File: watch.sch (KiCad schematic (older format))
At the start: 22 parts, among them P1 CONN_6, SW1 SW_PUSH, SW2 SW_PUSH, SW3 SW_PUSH, SW4 SW_PUSH, U1 nrf51822, U3 S25FL1-K, X1 16MHz, X2 32.768kHz

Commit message: Added .gitignore, finished midmount layout
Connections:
- net +3.3V: now also SW1.1, SW3.1; no longer SW1.2, SW3.2
- net CS_DISP: now also U1.10 (GPIO6/AIN7/AREF1); no longer U1.9 (GPIO5/AIN6)
- net CS_MEM: now also U1.48 (GPIO29); no longer U1.47 (GPIO28)
- net DC_DISP: now also U1.9 (GPIO5/AIN6); no longer U1.8 (GPIO4/AIN5)
- net DISP_EN: now also U1.11 (GPIO7); no longer U1.17 (GPIO11)
- net HOLD_MEM: now also U1.47 (GPIO28); no longer U1.48 (GPIO29)
- net MCU_CTS: now also U1.21 (GPIO15); no longer U1.25 (GPIO17)
- net MCU_RTS: now also U1.19 (GPIO13); no longer U1.18 (GPIO12)
- net MCU_RX: now also U1.22 (GPIO16); no longer U1.26 (GPIO18)
- net MCU_TX: now also U1.20 (GPIO14); no longer U1.22 (GPIO16)
- net MOSI: now also U1.6 (GPIO2/AIN3); no longer U1.3 (GPIO30)
- net RST_DISP: now also U1.8 (GPIO4/AIN5); no longer U1.7 (GPIO3/AIN4)
- net SCK: now also U1.7 (GPIO3/AIN4); no longer U1.4 (GPIO0/AREF0)
- net SW1: now also SW1.2, U1.17 (GPIO11); no longer SW1.1, U1.14 (GPIO8)
- net SW2: now also U1.4 (GPIO0/AREF0); no longer U1.6 (GPIO2/AIN3)
- net SW3: now also SW3.2, U1.18 (GPIO12); no longer SW3.1, U1.15 (GPIO9)
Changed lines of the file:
@@
 Text Label 5900 1950 0    60   ~ 0
 MISO
-Text Label 5900 1850 0    60   ~ 0
+Text Label 5900 1750 0    60   ~ 0
 CS_MEM
 Text Label 8150 1850 2    60   ~ 0
@@
 Text Label 9250 1750 0    60   ~ 0
 MISO
-Text Label 5900 1750 0    60   ~ 0
+Text Label 5900 1850 0    60   ~ 0
 HOLD_MEM
 Text Label 9250 1950 0    60   ~ 0
@@
 F 3 "" H 8600 5150 60  0000 C CNN
 	1    8600 5150
-	1    0    0    -1
+	-1   0    0    -1
 $EndComp
 $Comp
@@
 F 3 "" H 8600 5800 60  0000 C CNN
 	1    8600 5800
-	1    0    0    -1
+	-1   0    0    -1
 $EndComp
 $Comp
@@
 Text Label 8300 6100 2    60   ~ 0
 SW4
-Text Label 5900 3650 0    60   ~ 0
+Text Label 5900 3350 0    60   ~ 0
 SW1
-Text Label 5900 4150 0    60   ~ 0
+Text Label 5900 4550 0    60   ~ 0
 SW2
-Text Label 5900 3550 0    60   ~ 0
+Text Label 5900 3250 0    60   ~ 0
 SW3
 Text Label 5900 2150 0    60   ~ 0
@@
 Wire Wire Line
 	6500 5350 6500 4250
-Wire Wire Line
-	6500 4250 5900 4250
 Connection ~ 7000 5350
 $Comp
@@
 Wire Wire Line
 	6000 6900 6000 7200
-Text GLabel 6700 2650 2    60   Input ~ 0
+Text GLabel 6150 2950 2    60   Input ~ 0
 MCU_CTS
-Text GLabel 6700 3250 2    60   Input ~ 0
+Text GLabel 6150 3150 2    60   Input ~ 0
 MCU_RTS
-Text GLabel 6700 2800 2    60   Input ~ 0
+Text GLabel 6150 3050 2    60   Input ~ 0
 MCU_TX
-Text GLabel 6700 2500 2    60   Input ~ 0
+Text GLabel 6150 2850 2    60   Input ~ 0
 MCU_RX
 $Sheet
@@
 	1    0    0    -1
 $EndComp
+Text GLabel 6150 3850 2    60   Input ~ 0
+DC_DISP
 Text GLabel 6150 3950 2    60   Input ~ 0
-DC_DISP
+RST_DISP
+Text GLabel 6150 4450 2    60   Input ~ 0
+CS_DISP
+Wire Wire Line
+	6150 3950 5900 3950
+Wire Wire Line
+	5900 3850 6150 3850
 Text GLabel 6150 4050 2    60   Input ~ 0
-RST_DISP
-Text GLabel 6150 3850 2    60   Input ~ 0
-CS_DISP
+SCK
+Text GLabel 6150 4150 2    60   Input ~ 0
+MOSI
 Wire Wire Line
 	6150 4050 5900 4050
 Wire Wire Line
-	5900 3950 6150 3950
-Text GLabel 6150 4550 2    60   Input ~ 0
-SCK
-Text GLabel 6150 4350 2    60   Input ~ 0
-MOSI
-Wire Wire Line
-	6150 4550 5900 4550
-Wire Wire Line
-	6150 4350 5900 4350
-Text GLabel 6150 3350 2    60   Input ~ 0
+	6150 4150 5900 4150
+Text GLabel 6150 3750 2    60   Input ~ 0
 DISP_EN
-Wire Wire Line
-	6600 2750 5900 2750
-Wire Wire Line
-	6700 2650 6600 2650
-Wire Wire Line
-	6600 2650 6600 2750
-Wire Wire Line
-	6700 2500 6500 2500
-Wire Wire Line
-	6500 2500 6500 2650
-Wire Wire Line
-	6500 2650 5900 2650
-Wire Wire Line
-	5900 2850 6650 2850
-Wire Wire Line
-	6650 2850 6650 2800
-Wire Wire Line
-	6650 2800 6700 2800
-Wire Wire Line
-	6700 3250 5900 3250
 Text Label 5900 2050 0    60   ~ 0
 WP_MEM
 Wire Wire Line
-	6150 3850 5900 3850
-Wire Wire Line
-	5900 3350 6150 3350
+	6150 4450 5900 4450
+Wire Wire Line
+	5900 3750 6150 3750
 $Comp
 L GND #PWR015
@@
 	7600 2350 7950 2350
 Connection ~ 7950 2350
+Wire Wire Line
+	5900 2850 6150 2850
+Wire Wire Line
+	6150 3150 5900 3150
+Wire Wire Line
+	5900 3050 6150 3050
+Wire Wire Line
+	6150 2950 5900 2950
+Wire Wire Line
+	6500 4250 5900 4250
 $EndSCHEMATC

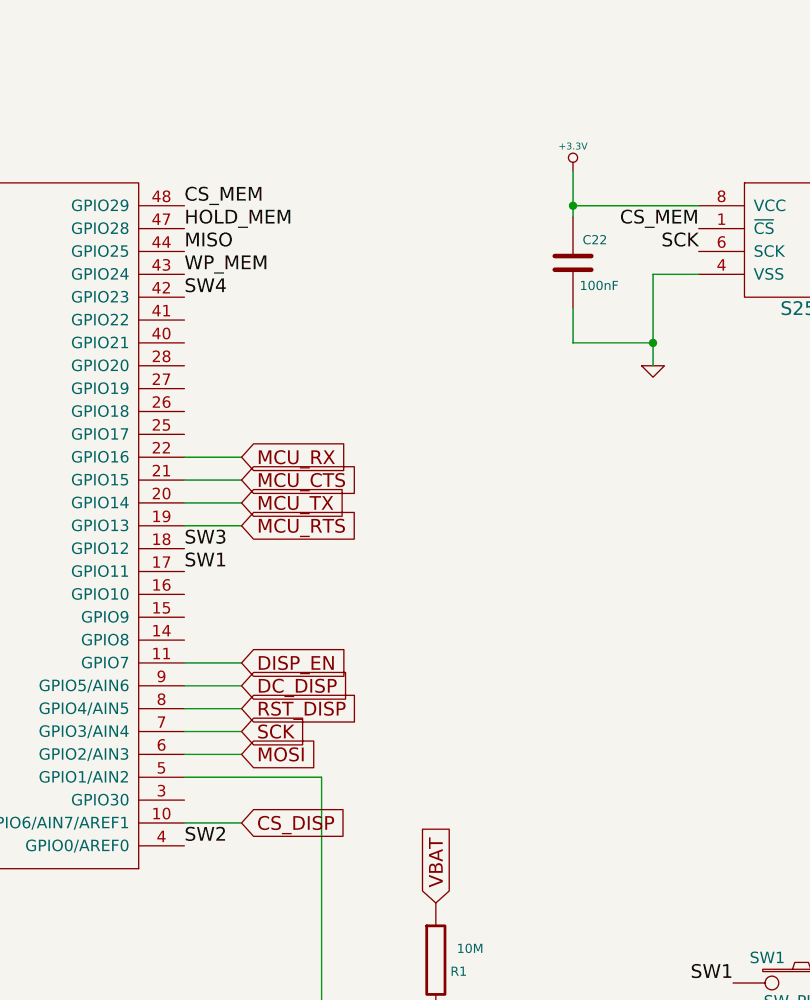
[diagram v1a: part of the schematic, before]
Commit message: Added testpoints, adjusted silkscreen texts
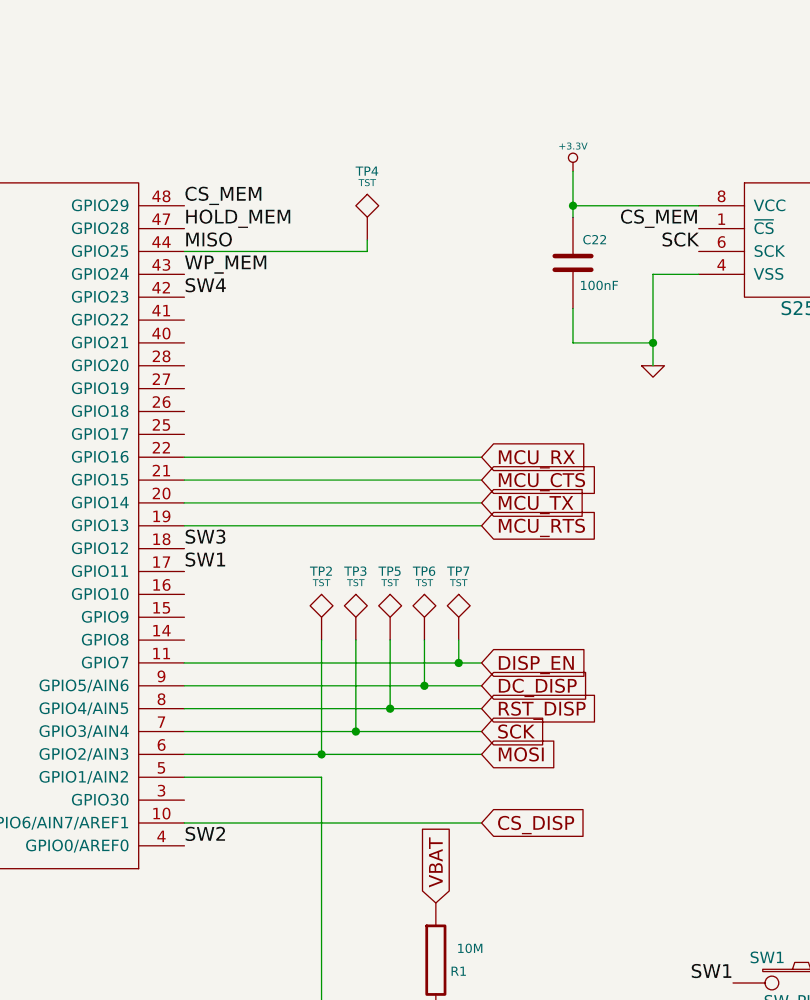
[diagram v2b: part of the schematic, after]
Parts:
- added TP2, TP3, TP4, TP5, TP6, TP7: TST, Measurement_Points:Measurement_Point_Round-SMD-Pad_Small, symbol TST
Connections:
- net DC_DISP: now also TP6.1
- net DISP_EN: now also TP7.1
- net MISO: now also TP4.1
- net MOSI: now also TP2.1
- net RST_DISP: now also TP5.1
- net SCK: now also TP3.1
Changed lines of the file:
@@
 	1    0    0    -1
 $EndComp
-Wire Wire Line
-	1700 1400 1700 1600
 NoConn ~ 3600 3100
 Wire Wire Line
@@
 Wire Wire Line
 	6000 6900 6000 7200
-Text GLabel 6150 2950 2    60   Input ~ 0
+Text GLabel 7200 2950 2    60   Input ~ 0
 MCU_CTS
-Text GLabel 6150 3150 2    60   Input ~ 0
+Text GLabel 7200 3150 2    60   Input ~ 0
 MCU_RTS
-Text GLabel 6150 3050 2    60   Input ~ 0
+Text GLabel 7200 3050 2    60   Input ~ 0
 MCU_TX
-Text GLabel 6150 2850 2    60   Input ~ 0
+Text GLabel 7200 2850 2    60   Input ~ 0
 MCU_RX
 $Sheet
@@
 	1    0    0    -1
 $EndComp
-Text GLabel 6150 3850 2    60   Input ~ 0
+Text GLabel 7200 3850 2    60   Input ~ 0
 DC_DISP
-Text GLabel 6150 3950 2    60   Input ~ 0
+Text GLabel 7200 3950 2    60   Input ~ 0
 RST_DISP
-Text GLabel 6150 4450 2    60   Input ~ 0
+Text GLabel 7200 4450 2    60   Input ~ 0
 CS_DISP
 Wire Wire Line
-	6150 3950 5900 3950
-Wire Wire Line
-	5900 3850 6150 3850
-Text GLabel 6150 4050 2    60   Input ~ 0
+	5900 3950 7200 3950
+Wire Wire Line
+	5900 3850 7200 3850
+Text GLabel 7200 4050 2    60   Input ~ 0
 SCK
-Text GLabel 6150 4150 2    60   Input ~ 0
+Text GLabel 7200 4150 2    60   Input ~ 0
 MOSI
 Wire Wire Line
-	6150 4050 5900 4050
-Wire Wire Line
-	6150 4150 5900 4150
-Text GLabel 6150 3750 2    60   Input ~ 0
+	5900 4050 7200 4050
+Wire Wire Line
+	5900 4150 7200 4150
+Text GLabel 7200 3750 2    60   Input ~ 0
 DISP_EN
 Text Label 5900 2050 0    60   ~ 0
 WP_MEM
 Wire Wire Line
-	6150 4450 5900 4450
-Wire Wire Line
-	5900 3750 6150 3750
+	7200 4450 5900 4450
+Wire Wire Line
+	5900 3750 7200 3750
 $Comp
 L GND #PWR015
@@
 Connection ~ 7950 2350
 Wire Wire Line
-	5900 2850 6150 2850
-Wire Wire Line
-	6150 3150 5900 3150
-Wire Wire Line
-	5900 3050 6150 3050
-Wire Wire Line
-	6150 2950 5900 2950
+	5900 2850 7200 2850
+Wire Wire Line
+	7200 3150 5900 3150
+Wire Wire Line
+	5900 3050 7200 3050
+Wire Wire Line
+	7200 2950 5900 2950
 Wire Wire Line
 	6500 4250 5900 4250
+$Comp
+L TST TP7
+U 1 1 548216F3
+P 7100 3650
+F 0 "TP7" H 7100 3950 40  0000 C CNN
+F 1 "TST" H 7100 3900 30  0000 C CNN
+F 2 "Measurement_Points:Measurement_Point_Round-SMD-Pad_Small" H 7100 3650 60  0001 C CNN
+F 3 "" H 7100 3650 60  0000 C CNN
+	1    7100 3650
+	1    0    0    -1
+$EndComp
+Wire Wire Line
+	7100 3650 7100 3750
+Connection ~ 7100 3750
+$Comp
+L TST TP6
+U 1 1 548223E0
+P 6950 3650
+F 0 "TP6" H 6950 3950 40  0000 C CNN
+F 1 "TST" H 6950 3900 30  0000 C CNN
+F 2 "Measurement_Points:Measurement_Point_Round-SMD-Pad_Small" H 6950 3650 60  0001 C CNN
+F 3 "" H 6950 3650 60  0000 C CNN
+	1    6950 3650
+	1    0    0    -1
+$EndComp
+Wire Wire Line
+	6950 3650 6950 3850
+Connection ~ 6950 3850
+$Comp
+L TST TP5
+U 1 1 54822867
+P 6800 3650
+F 0 "TP5" H 6800 3950 40  0000 C CNN
+F 1 "TST" H 6800 3900 30  0000 C CNN
+F 2 "Measurement_Points:Measurement_Point_Round-SMD-Pad_Small" H 6800 3650 60  0001 C CNN
+F 3 "" H 6800 3650 60  0000 C CNN
+	1    6800 3650
+	1    0    0    -1
+$EndComp
+Wire Wire Line
+	6800 3650 6800 3950
+Connection ~ 6800 3950
+$Comp
+L TST TP3
+U 1 1 54822938
+P 6650 3650
+F 0 "TP3" H 6650 3950 40  0000 C CNN
+F 1 "TST" H 6650 3900 30  0000 C CNN
+F 2 "Measurement_Points:Measurement_Point_Round-SMD-Pad_Small" H 6650 3650 60  0001 C CNN
+F 3 "" H 6650 3650 60  0000 C CNN
+	1    6650 3650
+	1    0    0    -1
+$EndComp
+Wire Wire Line
+	6650 3650 6650 4050
+Connection ~ 6650 4050
+$Comp
+L TST TP2
+U 1 1 54822ADA
+P 6500 3650
+F 0 "TP2" H 6500 3950 40  0000 C CNN
+F 1 "TST" H 6500 3900 30  0000 C CNN
+F 2 "Measurement_Points:Measurement_Point_Round-SMD-Pad_Small" H 6500 3650 60  0001 C CNN
+F 3 "" H 6500 3650 60  0000 C CNN
+	1    6500 3650
+	1    0    0    -1
+$EndComp
+Wire Wire Line
+	6500 3650 6500 4150
+Connection ~ 6500 4150
+$Comp
+L TST TP4
+U 1 1 54822DDC
+P 6700 1900
+F 0 "TP4" H 6700 2200 40  0000 C CNN
+F 1 "TST" H 6700 2150 30  0000 C CNN
+F 2 "Measurement_Points:Measurement_Point_Round-SMD-Pad_Small" H 6700 1900 60  0001 C CNN
+F 3 "" H 6700 1900 60  0000 C CNN
+	1    6700 1900
+	1    0    0    -1
+$EndComp
+Wire Wire Line
+	5900 1950 6700 1950
+Wire Wire Line
+	6700 1950 6700 1900
+Wire Wire Line
+	1700 1400 1700 1600
 $EndSCHEMATC

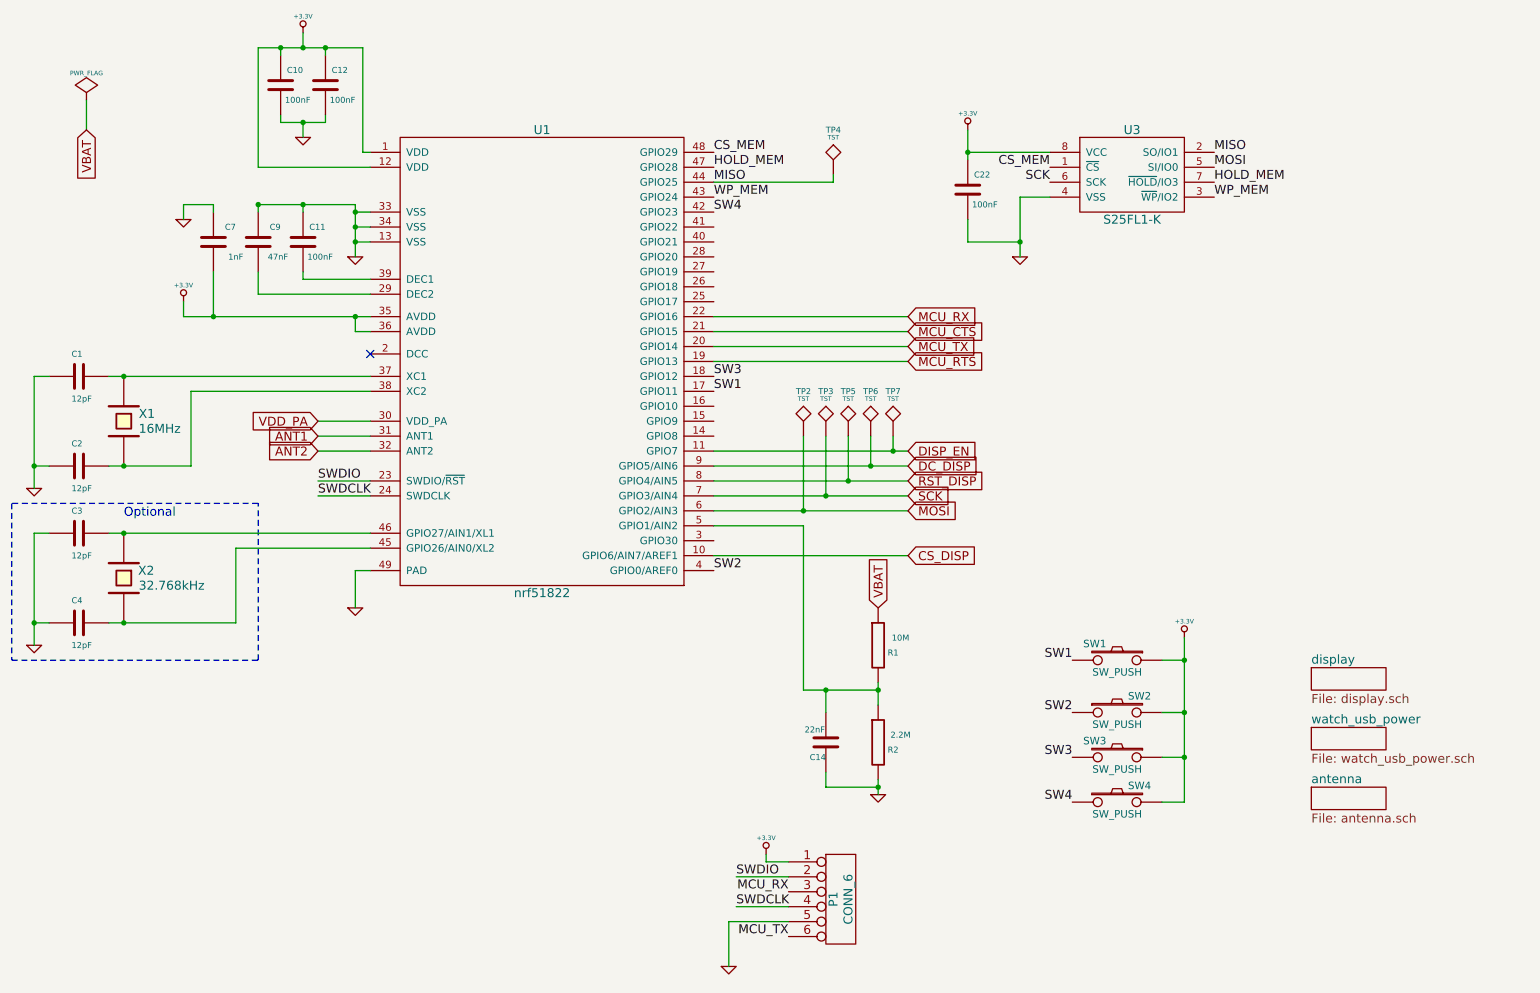
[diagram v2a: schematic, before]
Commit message: Added missing 2.2uF cap to LTC4063 LDO output, normalized capacitor values to micro and pico, removed units from component values
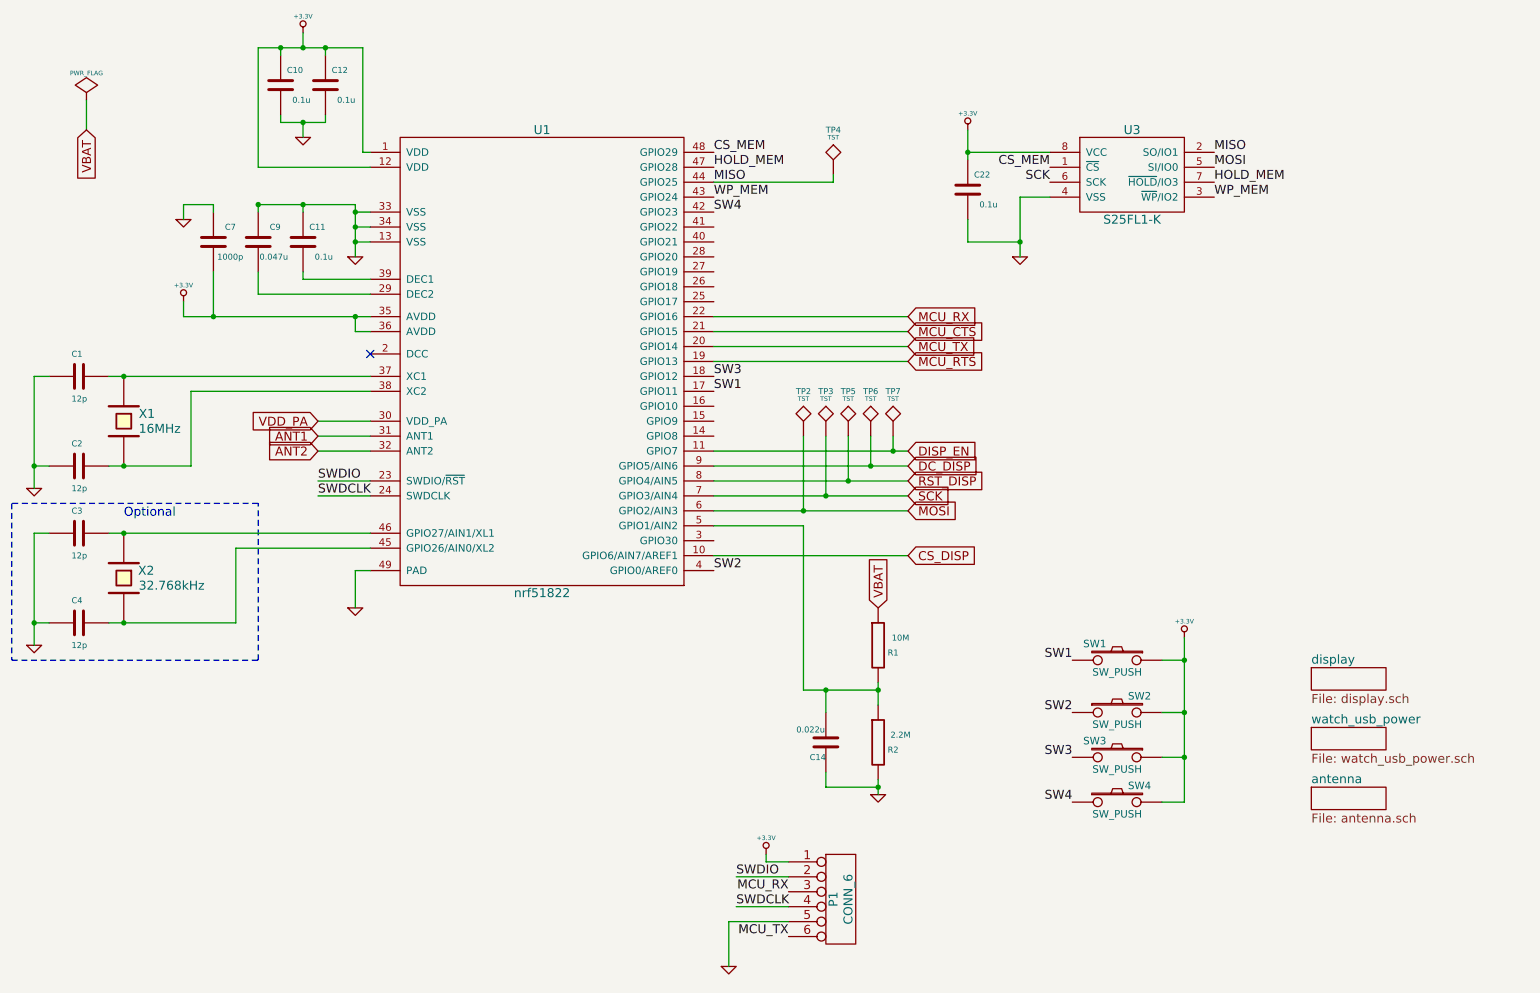
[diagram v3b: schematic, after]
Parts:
- C1, C2, C3, C4: value 12pF -> 12p
- C10, C11, C12, C22: value 100nF -> 0.1u
- C14: value 22nF -> 0.022u
- C7: value 1nF -> 1000p
- C9: value 47nF -> 0.047u
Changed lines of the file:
@@
 P 1650 3250
 F 0 "C1" V 1500 3200 40  0000 L CNN
-F 1 "12pF" V 1800 3200 40  0000 L CNN
+F 1 "12p" V 1800 3200 40  0000 L CNN
 F 2 "SMD_Packages:SMD-0603" H 1688 3100 30  0001 C CNN
 F 3 "" H 1650 3250 60  0000 C CNN
@@
 P 1650 3850
 F 0 "C2" V 1500 3800 40  0000 L CNN
-F 1 "12pF" V 1800 3800 40  0000 L CNN
+F 1 "12p" V 1800 3800 40  0000 L CNN
 F 2 "SMD_Packages:SMD-0603" H 1688 3700 30  0001 C CNN
 F 3 "" H 1650 3850 60  0000 C CNN
@@
 P 3300 1300
 F 0 "C12" H 3150 1200 40  0000 L CNN
-F 1 "100nF" H 3100 1400 40  0000 L CNN
+F 1 "0.1u" H 3100 1400 40  0000 L CNN
 F 2 "SMD_Packages:SMD-0603" H 3338 1150 30  0001 C CNN
 F 3 "" H 3300 1300 60  0000 C CNN
@@
 P 3000 1300
 F 0 "C10" H 2850 1200 40  0000 L CNN
-F 1 "100nF" H 2800 1400 40  0000 L CNN
+F 1 "0.1u" H 2800 1400 40  0000 L CNN
 F 2 "SMD_Packages:SMD-0603" H 3038 1150 30  0001 C CNN
 F 3 "" H 3000 1300 60  0000 C CNN
@@
 P 3150 2350
 F 0 "C11" H 3000 2250 40  0000 L CNN
-F 1 "100nF" H 2950 2450 40  0000 L CNN
+F 1 "0.1u" H 2950 2450 40  0000 L CNN
 F 2 "SMD_Packages:SMD-0603" H 3188 2200 30  0001 C CNN
 F 3 "" H 3150 2350 60  0000 C CNN
@@
 P 2850 2350
 F 0 "C9" H 2700 2250 40  0000 L CNN
-F 1 "47nF" H 2650 2450 40  0000 L CNN
+F 1 "0.047u" H 2650 2450 40  0000 L CNN
 F 2 "SMD_Packages:SMD-0603" H 2888 2200 30  0001 C CNN
 F 3 "" H 2850 2350 60  0000 C CNN
@@
 P 2550 2350
 F 0 "C7" H 2400 2250 40  0000 L CNN
-F 1 "1nF" H 2350 2450 40  0000 L CNN
+F 1 "1000p" H 2350 2450 40  0000 L CNN
 F 2 "SMD_Packages:SMD-0603" H 2588 2200 30  0001 C CNN
 F 3 "" H 2550 2350 60  0000 C CNN
@@
 P 1650 4300
 F 0 "C3" V 1500 4250 40  0000 L CNN
-F 1 "12pF" V 1800 4250 40  0000 L CNN
+F 1 "12p" V 1800 4250 40  0000 L CNN
 F 2 "SMD_Packages:SMD-0603" H 1688 4150 30  0001 C CNN
 F 3 "" H 1650 4300 60  0000 C CNN
@@
 P 1650 4900
 F 0 "C4" V 1500 4850 40  0000 L CNN
-F 1 "12pF" V 1800 4850 40  0000 L CNN
+F 1 "12p" V 1800 4850 40  0000 L CNN
 F 2 "SMD_Packages:SMD-0603" H 1688 4750 30  0001 C CNN
 F 3 "" H 1650 4900 60  0000 C CNN
@@
 P 6650 5700
 F 0 "C14" H 6650 5800 40  0000 L CNN
-F 1 "22nF" H 6656 5615 40  0000 L CNN
+F 1 "0.022u" H 6656 5615 40  0000 L CNN
 F 2 "SMD_Packages:SMD-0603" H 6688 5550 30  0001 C CNN
 F 3 "" H 6650 5700 60  0000 C CNN
@@
 P 7600 2000
 F 0 "C22" H 7450 1900 40  0000 L CNN
-F 1 "100nF" H 7400 2100 40  0000 L CNN
+F 1 "0.1u" H 7400 2100 40  0000 L CNN
 F 2 "SMD_Packages:SMD-0603" H 7638 1850 30  0001 C CNN
 F 3 "" H 7600 2000 60  0000 C CNN
